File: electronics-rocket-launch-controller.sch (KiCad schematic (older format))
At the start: 7 parts

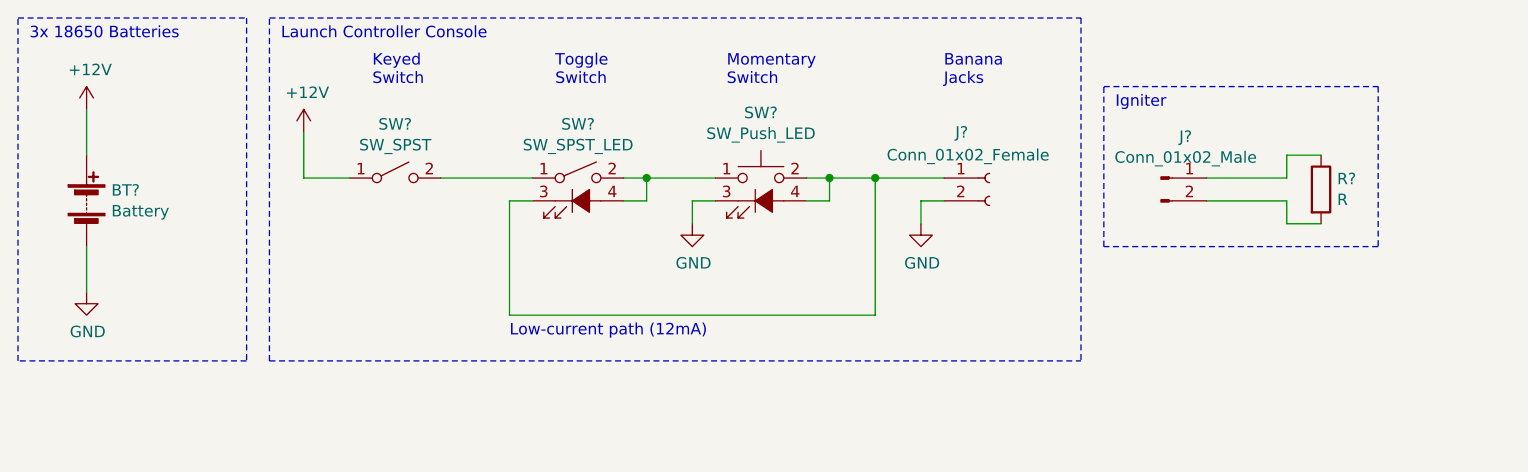
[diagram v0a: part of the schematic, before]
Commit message: Fix continuity test circuit.
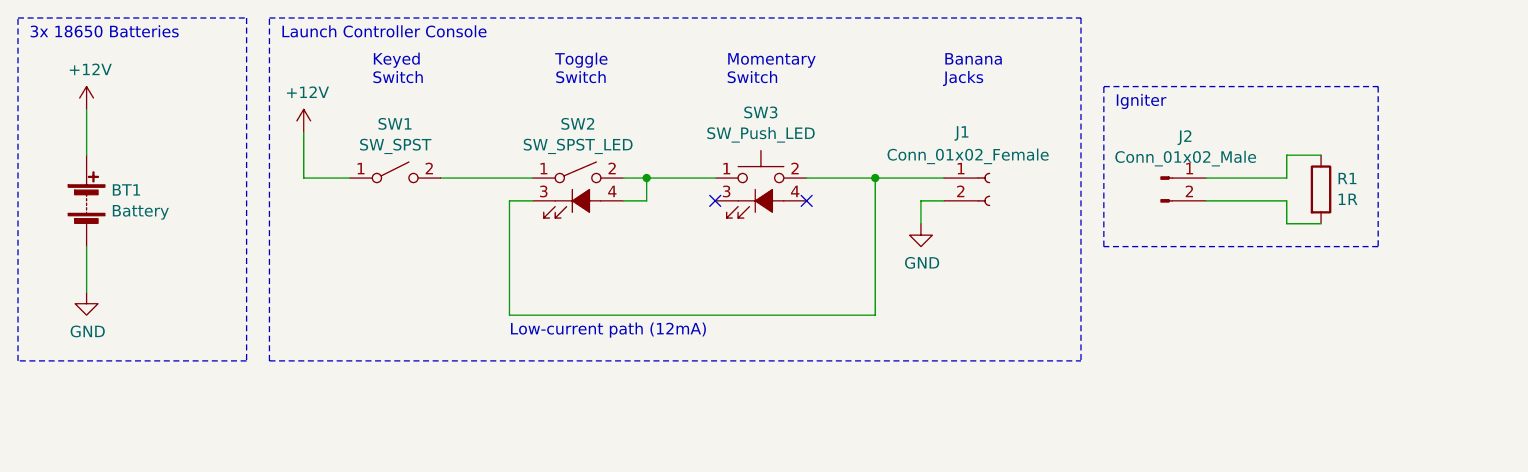
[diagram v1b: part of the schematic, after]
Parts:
- R1: renamed from R?; value R -> 1R
- gave numbers to parts that had none: 6
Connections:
- net GND: no longer SW3.3 (K)
- net at J1.1 (Pin_1), SW2.3 (K), SW3.2: no longer SW3.4 (A)
- no-connect marks 0 -> 2
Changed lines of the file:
@@
 1-0
 $Comp
-L power:+12V #PWR?
+L power:+12V #PWR01
 U 1 1 61F4986B
 P 3300 3900
-F 0 "#PWR?" H 3300 3750 50  0001 C CNN
+F 0 "#PWR01" H 3300 3750 50  0001 C CNN
 F 1 "+12V" H 3315 4073 50  0000 C CNN
 F 2 "" H 3300 3900 50  0001 C CNN
@@
 $EndComp
 $Comp
-L power:GND #PWR?
+L power:GND #PWR02
 U 1 1 61F49E29
 P 3300 4700
-F 0 "#PWR?" H 3300 4450 50  0001 C CNN
+F 0 "#PWR02" H 3300 4450 50  0001 C CNN
 F 1 "GND" H 3305 4527 50  0000 C CNN
 F 2 "" H 3300 4700 50  0001 C CNN
@@
 $EndComp
 $Comp
-L Device:Battery BT?
+L Device:Battery BT1
 U 1 1 61F4A275
 P 3300 4300
-F 0 "BT?" H 3408 4346 50  0000 L CNN
+F 0 "BT1" H 3408 4346 50  0000 L CNN
 F 1 "Battery" H 3408 4255 50  0000 L CNN
 F 2 "" V 3300 4360 50  0001 C CNN
@@
 $EndComp
 $Comp
-L Switch:SW_Push_LED SW?
+L Switch:SW_Push_LED SW3
 U 1 1 61F4BB5F
 P 6250 4300
-F 0 "SW?" H 6250 4685 50  0000 C CNN
+F 0 "SW3" H 6250 4685 50  0000 C CNN
 F 1 "SW_Push_LED" H 6250 4594 50  0000 C CNN
 F 2 "" H 6250 4600 50  0001 C CNN
@@
 $EndComp
 $Comp
-L Switch:SW_SPST_LED SW?
+L Switch:SW_SPST_LED SW2
 U 1 1 61F4C879
 P 5450 4300
-F 0 "SW?" H 5450 4635 50  0000 C CNN
+F 0 "SW2" H 5450 4635 50  0000 C CNN
 F 1 "SW_SPST_LED" H 5450 4544 50  0000 C CNN
 F 2 "" H 5450 4600 50  0001 C CNN
@@
 $EndComp
 $Comp
-L Switch:SW_SPST SW?
+L Switch:SW_SPST SW1
 U 1 1 61F4CEA6
 P 4650 4200
-F 0 "SW?" H 4650 4435 50  0000 C CNN
+F 0 "SW1" H 4650 4435 50  0000 C CNN
 F 1 "SW_SPST" H 4650 4344 50  0000 C CNN
 F 2 "" H 4650 4200 50  0001 C CNN
@@
 $EndComp
 $Comp
-L Device:R R?
+L Device:R R1
 U 1 1 61F4DF28
 P 8700 4250
-F 0 "R?" H 8770 4296 50  0000 L CNN
-F 1 "R" H 8770 4205 50  0000 L CNN
+F 0 "R1" H 8770 4296 50  0000 L CNN
+F 1 "1R" H 8770 4205 50  0000 L CNN
 F 2 "" V 8630 4250 50  0001 C CNN
 F 3 "~" H 8700 4250 50  0001 C CNN
@@
 $EndComp
 $Comp
-L Connector:Conn_01x02_Female J?
+L Connector:Conn_01x02_Female J1
 U 1 1 61F4E830
 P 7250 4200
-F 0 "J?" H 7100 4400 50  0000 L CNN
+F 0 "J1" H 7100 4400 50  0000 L CNN
 F 1 "Conn_01x02_Female" H 6800 4300 50  0000 L CNN
 F 2 "" H 7250 4200 50  0001 C CNN
@@
 $EndComp
 $Comp
-L Connector:Conn_01x02_Male J?
+L Connector:Conn_01x02_Male J2
 U 1 1 61F4F3ED
 P 8000 4200
-F 0 "J?" H 8108 4381 50  0000 C CNN
+F 0 "J2" H 8108 4381 50  0000 C CNN
 F 1 "Conn_01x02_Male" H 8108 4290 50  0000 C CNN
 F 2 "" H 8000 4200 50  0001 C CNN
@@
 $EndComp
 $Comp
-L power:+12V #PWR?
+L power:+12V #PWR03
 U 1 1 61F54412
 P 4250 4000
-F 0 "#PWR?" H 4250 3850 50  0001 C CNN
+F 0 "#PWR03" H 4250 3850 50  0001 C CNN
 F 1 "+12V" H 4265 4173 50  0000 C CNN
 F 2 "" H 4250 4000 50  0001 C CNN
@@
 $EndComp
 $Comp
-L power:GND #PWR?
+L power:GND #PWR04
 U 1 1 61F58FF2
 P 6950 4400
-F 0 "#PWR?" H 6950 4150 50  0001 C CNN
+F 0 "#PWR04" H 6950 4150 50  0001 C CNN
 F 1 "GND" H 6955 4227 50  0000 C CNN
 F 2 "" H 6950 4400 50  0001 C CNN
@@
 	1    0    0    -1
 $EndComp
-$Comp
-L power:GND #PWR?
-U 1 1 61F5A6AF
-P 5950 4400
-F 0 "#PWR?" H 5950 4150 50  0001 C CNN
-F 1 "GND" H 5955 4227 50  0000 C CNN
-F 2 "" H 5950 4400 50  0001 C CNN
-F 3 "" H 5950 4400 50  0001 C CNN
-	1    5950 4400
-	1    0    0    -1
-$EndComp
 Wire Wire Line
 	3300 4500 3300 4700
@@
 	5650 4200 5750 4200
 Wire Wire Line
-	6450 4200 6550 4200
-Wire Wire Line
 	7050 4300 6950 4300
-Wire Wire Line
-	6550 4200 6550 4300
-Wire Wire Line
-	6550 4300 6450 4300
 Wire Wire Line
 	6750 4200 7050 4200
@@
 	5750 4200 6050 4200
 Wire Wire Line
-	6050 4300 5950 4300
-Wire Wire Line
-	5950 4300 5950 4400
-Wire Wire Line
 	6950 4300 6950 4400
 Wire Wire Line
@@
 Wire Wire Line
 	6750 4800 6750 4200
-Wire Wire Line
-	6750 4200 6550 4200
 Connection ~ 6750 4200
-Connection ~ 6550 4200
 Wire Wire Line
 	8200 4200 8550 4200
@@
 Wire Notes Line
 	4100 5000 7650 5000
+Wire Wire Line
+	6450 4200 6750 4200
+NoConn ~ 6050 4300
+NoConn ~ 6450 4300
 $EndSCHEMATC
